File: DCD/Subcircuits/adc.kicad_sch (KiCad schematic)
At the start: 17 parts, among them U1 AD4630-24BBCZ, U2 ADR4550BRZ

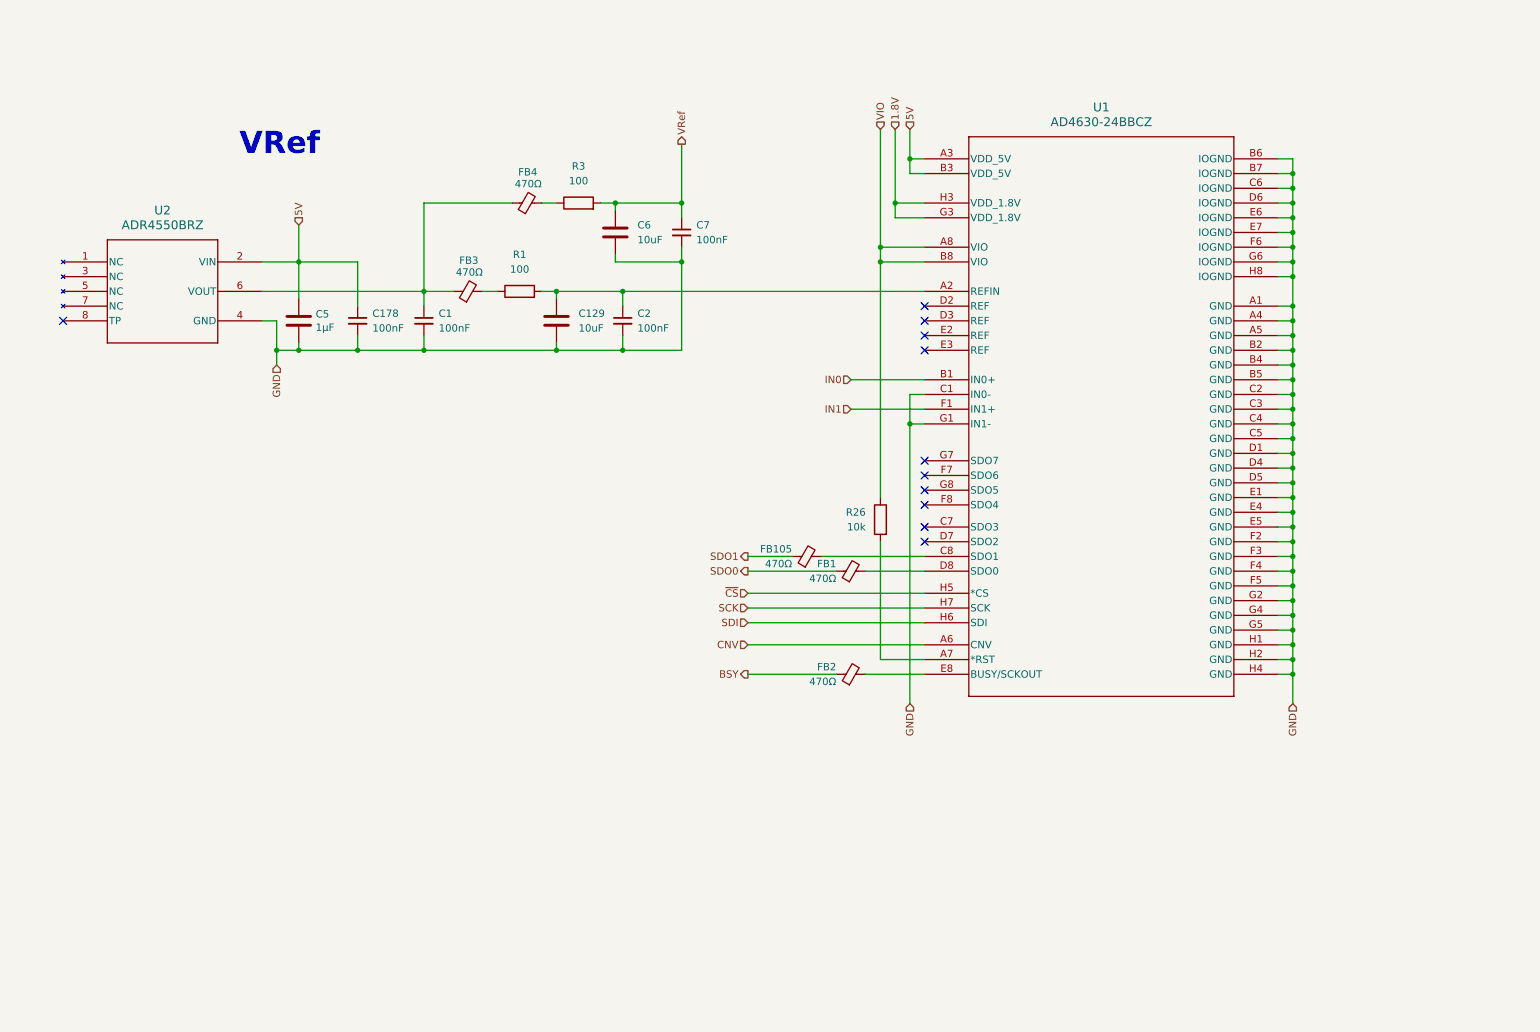
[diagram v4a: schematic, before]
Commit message: Progress on the implementation of the DAC driver
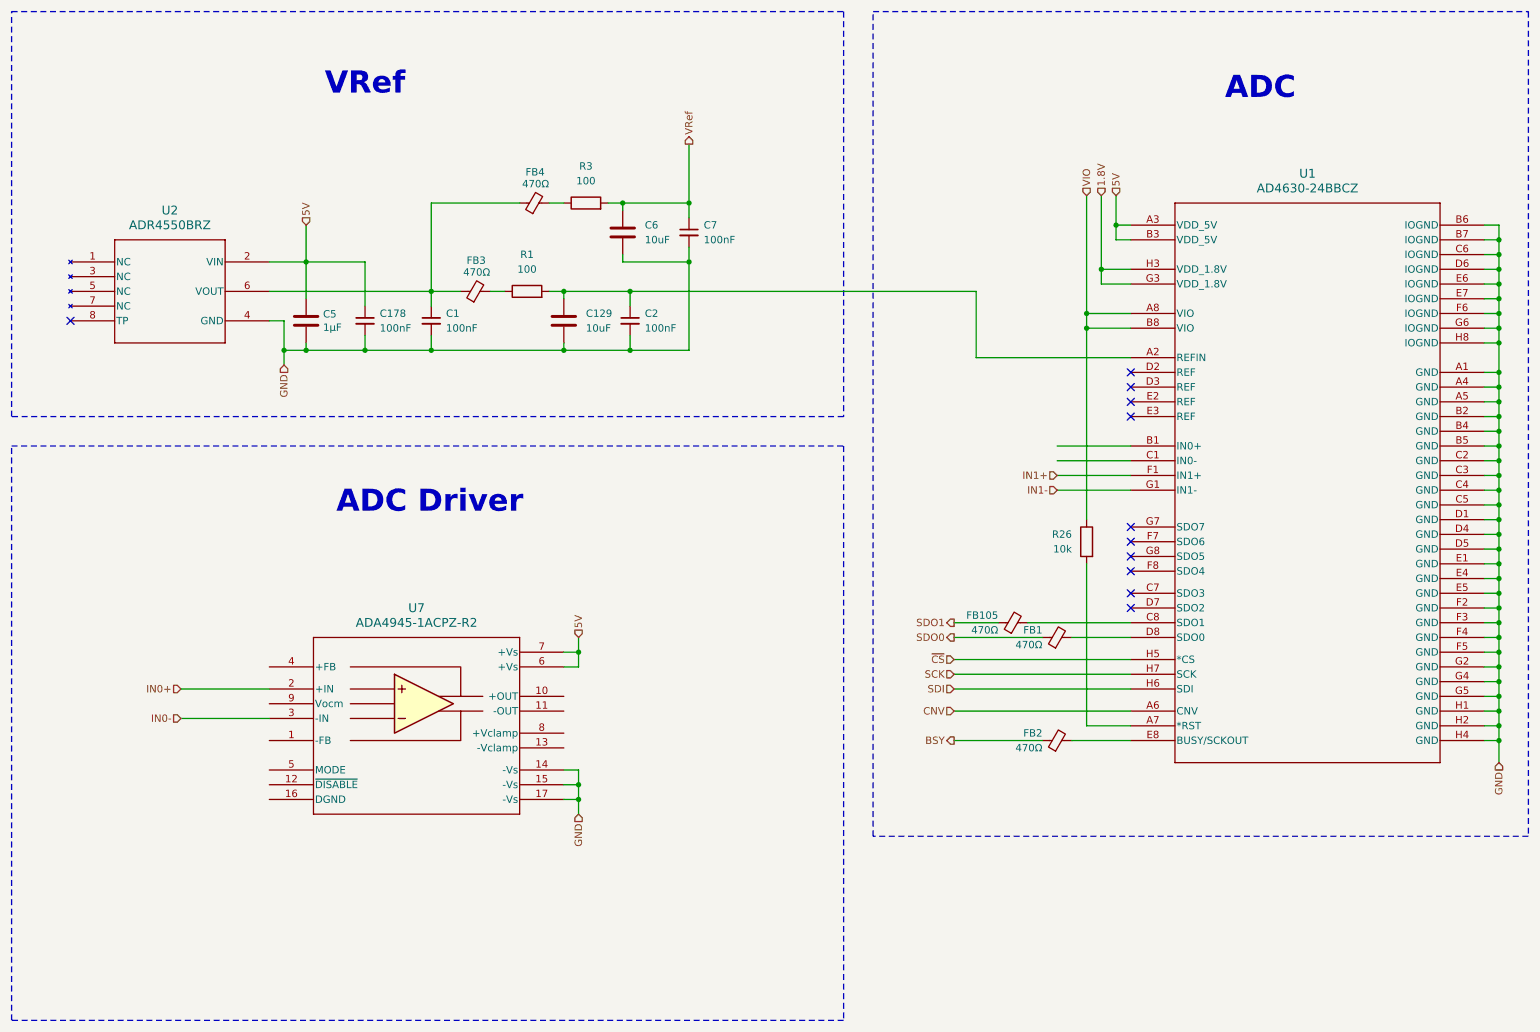
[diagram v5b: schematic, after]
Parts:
- added U7: ADA4945-1ACPZ-R2, LFCSP16_ADA4945-1ACPZ-R2_ADI, symbol custom_components:ADA4945-1ACPZ-R2
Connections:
- net 5V: now also U7.6 (+Vs), U7.7 (+Vs)
- net GND: now also U7.14 (-Vs), U7.15 (-Vs), U7.17 (-Vs); no longer U1.C1 (IN0-), U1.G1 (IN1-)
- net IN0: no longer names the net of U1.B1 (IN0+)
- net IN1 renamed IN1+
- new net IN0+: U7.2 (+IN)
- new net IN0-: U7.3 (-IN)
- new net IN1-: U1.G1 (IN1-)
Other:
- note added: "ADC"
- note added: "ADC Driver"
- moved on the sheet: C1, C129, C178, C2, C5, C6, C7, FB1, FB105, FB2, FB3, FB4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

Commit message: Fixed the switches, finished the adc amplifier, missing the filer to adc
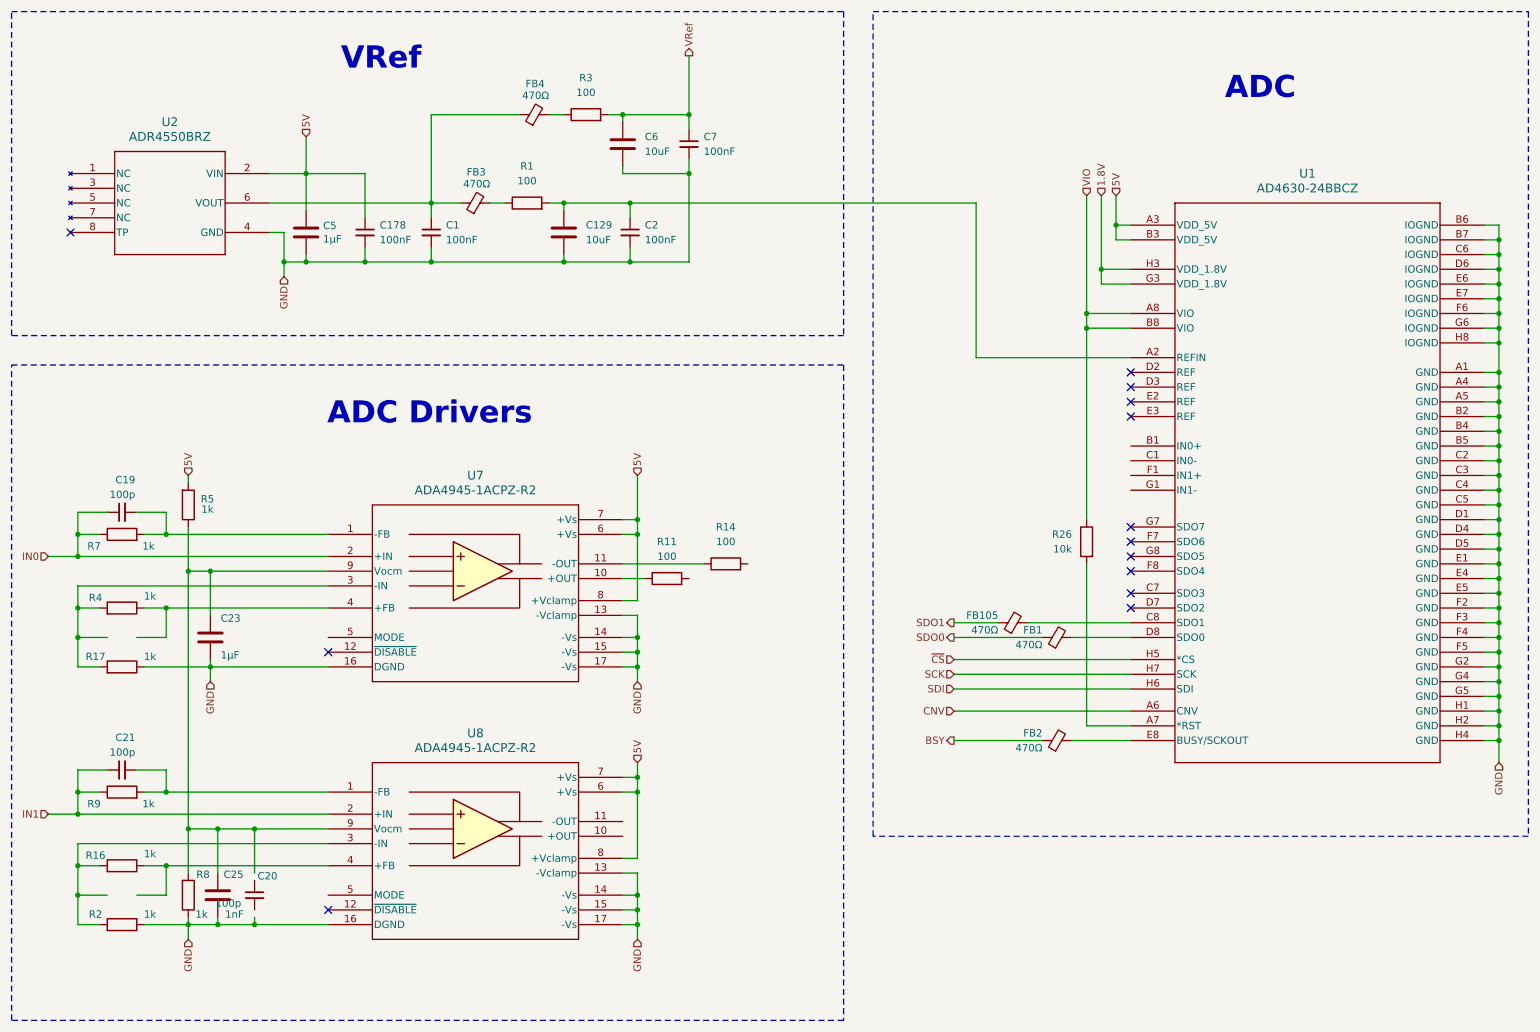
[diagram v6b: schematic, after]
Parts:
- added C19, C20, C21: 100p, Capacitor_SMD:C_0603_1608Metric, symbol Device:C_Small
- added C23: 1µF, Capacitor_SMD:C_0603_1608Metric, symbol Device:C
- added C25: 1nF, Capacitor_SMD:C_0603_1608Metric, symbol Device:C
- added R11, R14: 100, Resistor_SMD:R_0603_1608Metric, symbol Device:R
- added R16, R17, R2, R4, R5, R7, R8, R9: 1k, Resistor_SMD:R_0603_1608Metric, symbol Device:R
- added U8: ADA4945-1ACPZ-R2, LFCSP16_ADA4945-1ACPZ-R2_ADI, symbol custom_components:ADA4945-1ACPZ-R2
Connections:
- net 5V: now also U7.8 (+Vclamp), R5.2, U8.6 (+Vs), U8.7 (+Vs), U8.8 (+Vclamp)
- net GND: now also U7.13 (-Vclamp), U7.16 (DGND), C23.2, C25.2, R17.1, R2.1, R8.1, U8.13 (-Vclamp), U8.14 (-Vs), U8.15 (-Vs), U8.16 (DGND), U8.17 (-Vs)
- net at U7.1 (-FB): now also C19.2, R7.2
- net at U7.10 (+OUT): now also R11.1
- net at U7.11 (-OUT): now also R14.1
- net at U7.4 (+FB): now also R4.1
- net at U7.9 (Vocm): now also C23.1, C25.1, R5.1, R8.2, U8.9 (Vocm)
- net IN0+ renamed IN0
- net IN0: now also C19.1, R7.1
- net IN0-: no longer names the net of U7.3 (-IN)
- net IN0-: now also R17.2, R4.2
- net IN1+: no longer names the net of U1.F1 (IN1+)
- net IN1-: no longer names the net of U1.G1 (IN1-)
- new net: C21.2, R9.2, U8.1 (-FB)
- new net: R16.2, R2.2, U8.3 (-IN)
- new net: R16.1, U8.4 (+FB)
- new net IN1: C21.1, R9.1, U8.2 (+IN)
- no-connect marks 11 -> 13
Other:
- note added: "ADC Drivers"
- note removed: "ADC Driver"
- moved on the sheet: C1, C129, C178, C2, C5, C6, C7, FB3, FB4, R1, R3, U2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

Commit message: Finished the schematics. Fixed the comments that we recieved
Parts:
- added C14, C16: 100p, Capacitor_SMD:C_0603_1608Metric, symbol Device:C_Small
- added C27, C28, C29, C30: 1nF, Capacitor_SMD:C_0603_1608Metric, symbol Device:C
- added R13, R15: 100, Resistor_SMD:R_0603_1608Metric, symbol Device:R
- added R9: 1k, Resistor_SMD:R_0603_1608Metric, symbol Device:R
- C18: renamed from C25; Link https://nl.mouser.com/ProductDetail/KEMET/C0603X102KCRAC331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 -> https://www.mouser.com/ProductDetail/Murata-Electronics/GCM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; Order number 80-C0603X102KCR3316 -> 81-GCM1885C2A102FA6D; Part number C0603X102KCRAC3316 -> GCM1885C2A102FA16D
- renumbered C19 to C13, C21 to C15, C23 to C17, C20 to C19, C5 to C20, C178 to C21, C1 to C22, C129 to C23, C6 to C24, C2 to C25, C7 to C26, FB3 to FB5, FB4 to FB6, FB105 to FB7, FB1 to FB8, FB2 to FB9, R7 to R1, R1 to R10, R3 to R11, R11 to R12, R26 to R16, R4 to R2, R17 to R3, R9 to R4, R16 to R5, R2 to R6, R5 to R7, U2 to U4, U7 to U5, U8 to U6, U1 to U7
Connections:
- net 5V: now also R9.2
- net GND: now also C19.2, C27.2, C28.2, C29.2, C30.2
- net at U6.10 (+OUT): now also R13.1
- net at U6.11 (-OUT): now also R15.1
- net at R5.2, R6.2, U6.3 (-IN): now also C16.1
- net at R5.1, U6.4 (+FB): now also C16.2
- net at U6.5 (MODE): now also U5.5 (MODE), R9.1
- net at C17.1, C18.1, R7.1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: now also C19.1
- net at R2.1, U5.4 (+FB): now also C14.2
- net at R2.2, R3.2, U5.3 (-IN): now also C14.1
- net at R14.2: now also U7.C1 (IN0-), C29.1
- net at R12.2: now also U7.B1 (IN0+), C27.1
- net at U7.F1 (IN1+): now also C28.1, R13.2
- net at U7.G1 (IN1-): now also C30.1, R15.2
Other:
- moved on the sheet: C17, R12, R14, R16, U5, U6

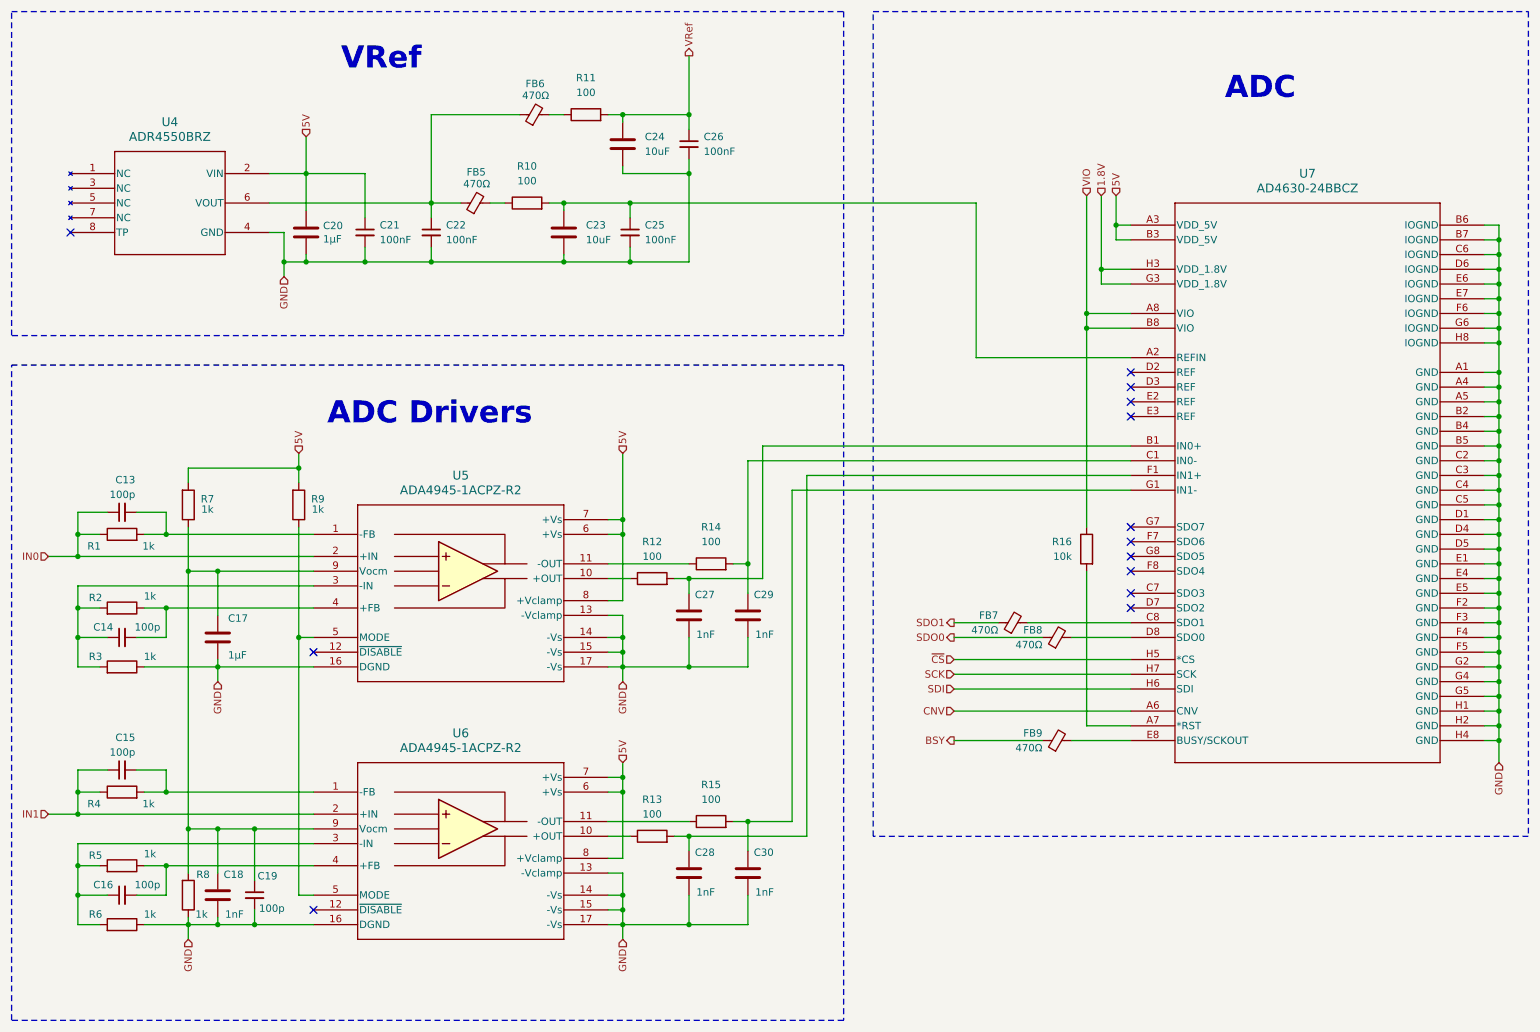
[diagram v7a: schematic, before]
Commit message: Finished
Final touches, PSUs filtering, external connections, psu connections for
the negative voltage, and the DAC higher voltage, and the negative
voltage. Added an external connection directely to the DAC.
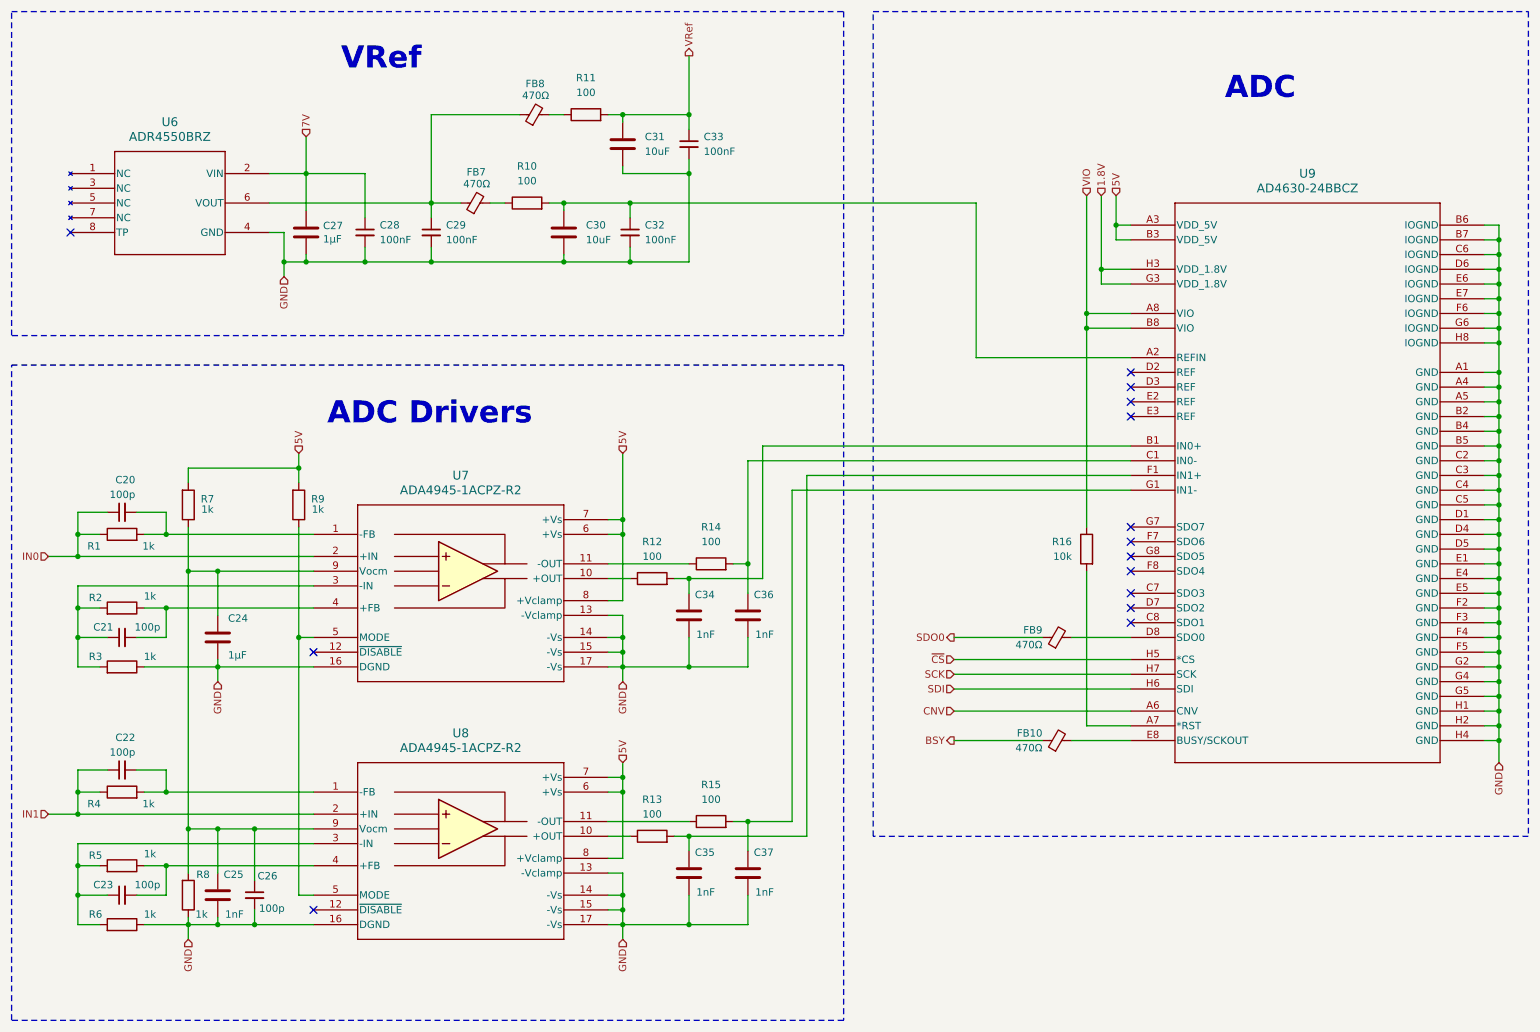
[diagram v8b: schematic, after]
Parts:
- removed FB7: 470Ω, Inductor_SMD:L_0603_1608Metric, symbol Device:FerriteBead_Small
- renumbered C13 to C20, C14 to C21, C15 to C22, C16 to C23, C17 to C24, C18 to C25, C19 to C26, C20 to C27, C21 to C28, C22 to C29, C23 to C30, C24 to C31, C25 to C32, C26 to C33, C27 to C34, C28 to C35, C29 to C36, C30 to C37, FB9 to FB10, FB5 to FB7, FB6 to FB8, FB8 to FB9, U4 to U6, U5 to U7, U6 to U8, U7 to U9
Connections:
- net 5V: no longer C27.1, C28.1, U6.2 (VIN)
- new net 7V: C27.1, C28.1, U6.2 (VIN)
- no-connect marks 13 -> 14
